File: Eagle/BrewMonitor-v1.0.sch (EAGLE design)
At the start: 14 parts, among them U1 ATMEGA328P_PDIP

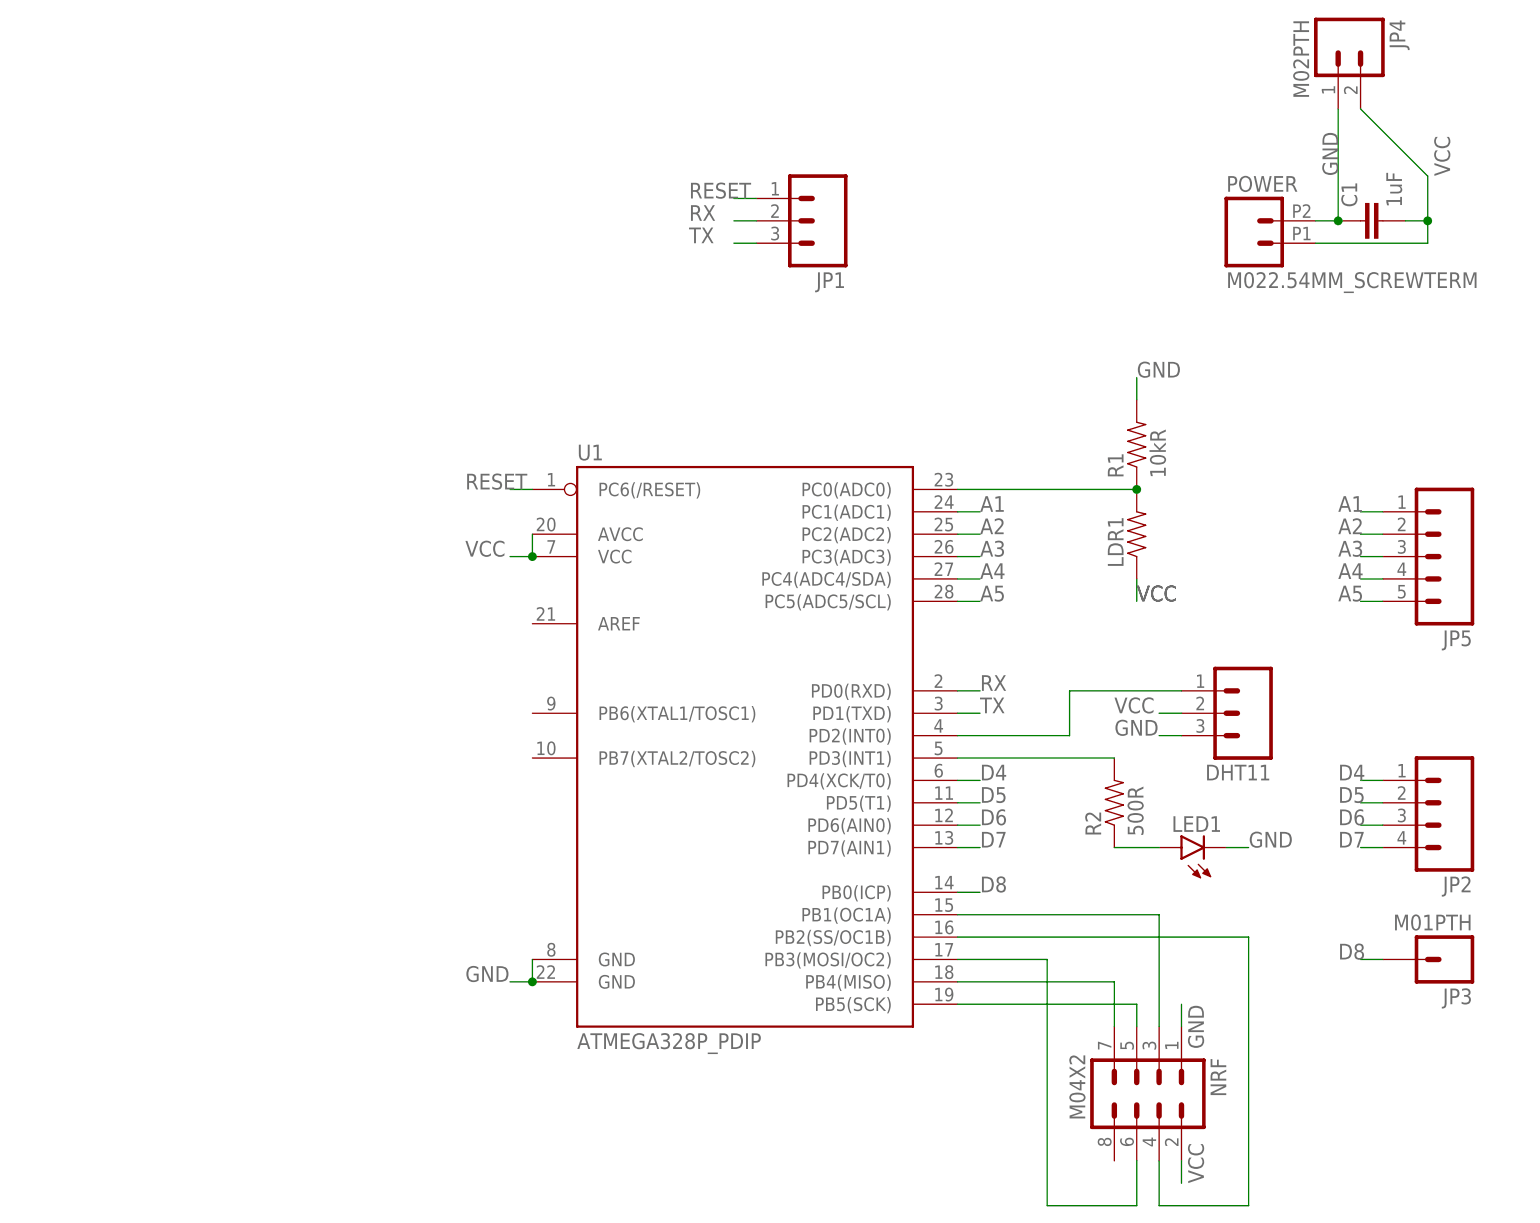
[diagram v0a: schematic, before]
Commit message: Updated Eagle Schematic for the correct parts and made net connections. The brd file still needs updating.
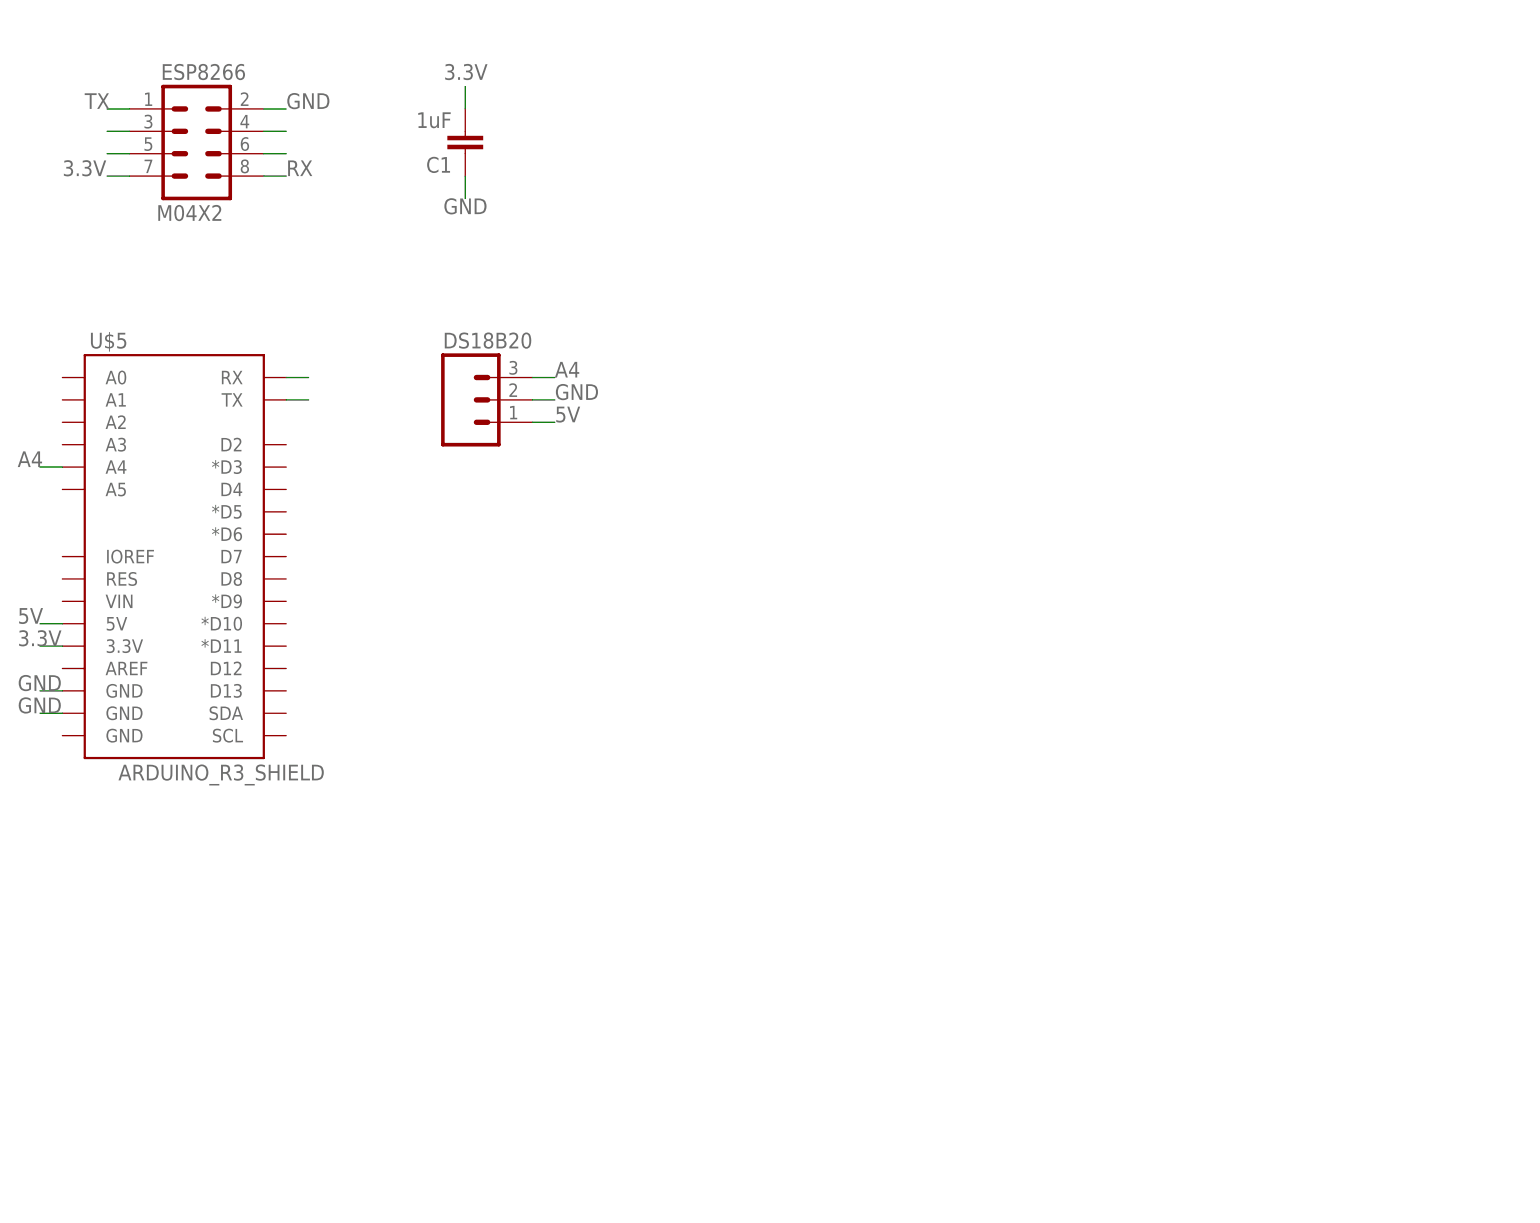
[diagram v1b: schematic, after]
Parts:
- removed DHT11, JP1: (no value), SparkFun-Connectors:M03PTH
- removed JP2: (no value), SparkFun-Connectors:M04PTH
- removed JP3: M01PTH, SparkFun-Connectors:M01PTH
- removed JP4: M02PTH, SparkFun-Connectors:M02PTH
- removed JP5: (no value), SparkFun-Connectors:M05PTH
- removed LDR1: (no value), SparkFun-Passives:RESISTORKIT
- removed LED1: (no value), SparkFun-LED:LED3MM
- removed NRF: M04X2, SparkFun-Connectors:M04X2
- removed POWER: M022.54MM_SCREWTERM, SparkFun-Connectors:M022.54MM_SCREWTERM
- removed R1: 10kR, SparkFun-Passives:RESISTORKIT
- removed R2: 500R, SparkFun-Passives:RESISTORKIT
- removed U1: ATMEGA328P_PDIP, SparkFun-DigitalIC:ATMEGA328P_PDIP
- added DS18B20: (no value), SparkFun-Connectors:M03SCREW
- added ESP8266: M04X2, SparkFun-Connectors:M04X2
- added U$5: ARDUINO_R3_SHIELD, SparkFun-Boards:ARDUINO_R3_SHIELD
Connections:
- removed net A1: JP5.1, U1.PC1(ADC1)
- removed net A2: JP5.2, U1.PC2(ADC2)
- removed net A3: JP5.3, U1.PC3(ADC3)
- removed net A5: JP5.5, U1.PC5(ADC5/SCL)
- removed net D4: JP2.1, U1.PD4(XCK/T0)
- removed net D5: JP2.2, U1.PD5(T1)
- removed net D6: JP2.3, U1.PD6(AIN0)
- removed net D7: JP2.4, U1.PD7(AIN1)
- removed net D8: JP3.1, U1.PB0(ICP)
- removed net N$1: LDR1.2, R1.1, U1.PC0(ADC0)
- removed net N$10: NRF.6, U1.PB3(MOSI/OC2)
- removed net N$2: LED1.A, R2.1
- removed net N$3: DHT11.1, U1.PD2(INT0)
- removed net N$4: R2.2, U1.PD3(INT1)
- removed net N$5: NRF.3, U1.PB1(OC1A)
- removed net N$6: NRF.4, U1.PB2(SS/OC1B)
- removed net N$7: NRF.5, U1.PB5(SCK)
- removed net N$9: NRF.7, U1.PB4(MISO)
- removed net RESET: JP1.1, U1.PC6(/RESET)
- removed net VCC: C1.2, DHT11.2, JP4.2, LDR1.1, NRF.2, POWER.1, U1.AVCC, U1.VCC
- new net 3.3V: C1.2, ESP8266.7, U$5.3.3V
- new net 5V: DS18B20.1, U$5.5V
- new net N$11: ESP8266.3
- new net N$12: ESP8266.5
- new net N$15: ESP8266.4
- new net N$16: ESP8266.6
- net A4: now also DS18B20.3, U$5.A4; no longer JP5.4, U1.PC4(ADC4/SDA)
- net GND: now also DS18B20.2, ESP8266.2, U$5.GND@1, U$5.GND@2; no longer DHT11.3, JP4.1, LED1.C, NRF.1, POWER.2, R1.2, U1.GND@1, U1.GND@2
- net RX: now also ESP8266.8, U$5.RX; no longer JP1.2, U1.PD0(RXD)
- net TX: now also ESP8266.1, U$5.TX; no longer JP1.3, U1.PD1(TXD)
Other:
- moved on the sheet: C1

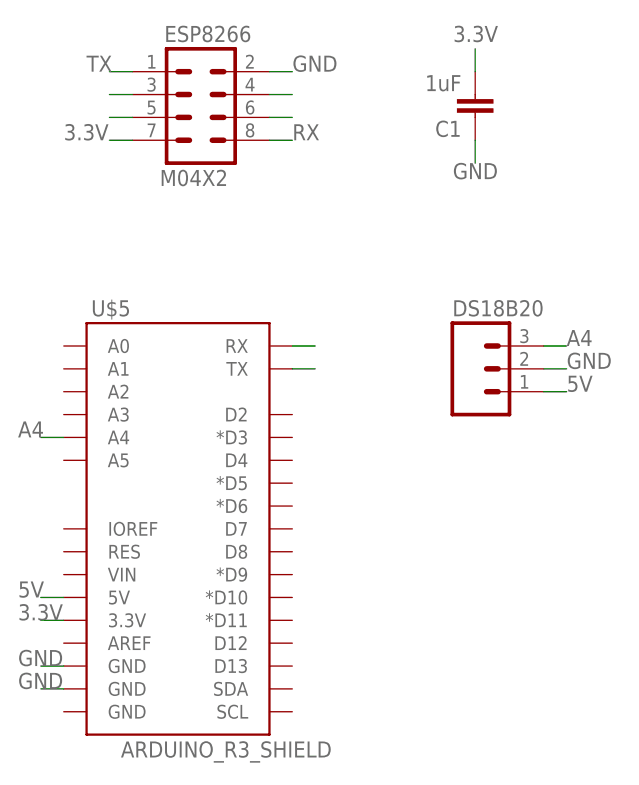
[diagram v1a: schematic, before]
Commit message: Updated Schematic and Board files. Circuit now complete.
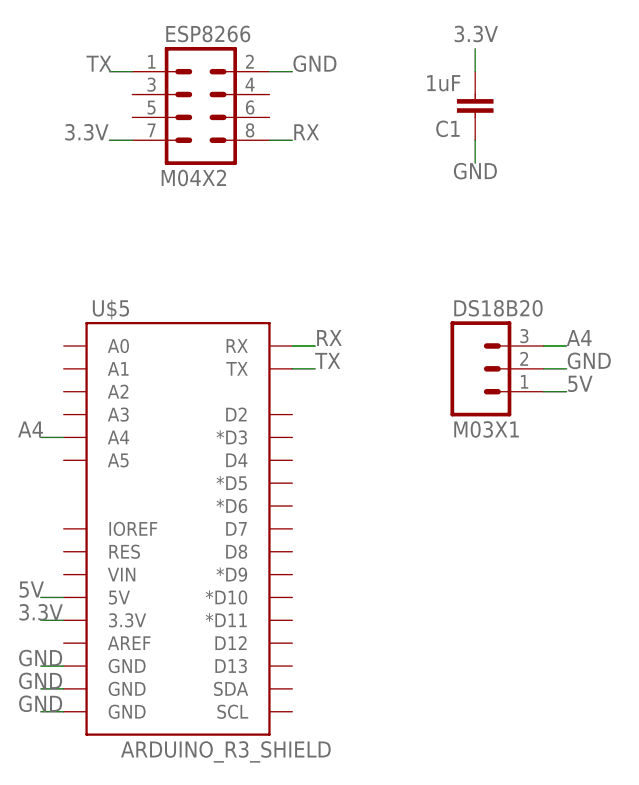
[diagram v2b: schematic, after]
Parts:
- DS18B20: value (none) -> M03X1
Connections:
- removed net N$11: ESP8266.3
- removed net N$12: ESP8266.5
- removed net N$15: ESP8266.4
- removed net N$16: ESP8266.6
- net GND: now also U$5.GND@0
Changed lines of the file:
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@@
 <part name="C1" library="SparkFun-Passives" deviceset="CAP" device="PTH" value="1uF"/>
 <part name="U$5" library="SparkFun-Boards" deviceset="ARDUINO_R3_SHIELD" device=""/>
-<part name="DS18B20" library="SparkFun-Connectors" deviceset="M03" device="SCREW"/>
+<part name="DS18B20" library="SparkFun-Connectors" deviceset="M03" device="SCREW" value="M03X1"/>
 </parts>
 <sheets>
@@
 <net name="GND" class="0">
 <segment>
-<pinref part="C1" gate="G$1" pin="1"/>
-<label x="48.26" y="106.68" size="1.778" layer="95" rot="R180"/>
-<wire x1="45.72" y1="109.22" x2="45.72" y2="106.68" width="0.1524" layer="91"/>
+<pinref part="DS18B20" gate="G$1" pin="2"/>
+<wire x1="53.34" y1="83.82" x2="55.88" y2="83.82" width="0.1524" layer="91"/>
+<label x="55.88" y="83.82" size="1.778" layer="95"/>
+</segment>
+<segment>
+<pinref part="U$5" gate="G$1" pin="GND@0"/>
+<wire x1="0" y1="45.72" x2="-2.54" y2="45.72" width="0.1524" layer="91"/>
+<label x="-5.08" y="45.72" size="1.778" layer="95"/>
 </segment>
 <segment>
@@
 </segment>
 <segment>
-<pinref part="U$5" gate="G$1" pin="GND@1"/>
-<wire x1="0" y1="48.26" x2="-2.54" y2="48.26" width="0.1524" layer="91"/>
-<label x="-5.08" y="48.26" size="1.778" layer="95"/>
+<pinref part="C1" gate="G$1" pin="1"/>
+<label x="48.26" y="106.68" size="1.778" layer="95" rot="R180"/>
+<wire x1="45.72" y1="109.22" x2="45.72" y2="106.68" width="0.1524" layer="91"/>
 </segment>
 <segment>
@@
 </segment>
 <segment>
-<pinref part="DS18B20" gate="G$1" pin="2"/>
-<wire x1="53.34" y1="83.82" x2="55.88" y2="83.82" width="0.1524" layer="91"/>
-<label x="55.88" y="83.82" size="1.778" layer="95"/>
+<pinref part="U$5" gate="G$1" pin="GND@1"/>
+<wire x1="0" y1="48.26" x2="-2.54" y2="48.26" width="0.1524" layer="91"/>
+<label x="-5.08" y="48.26" size="1.778" layer="95"/>
 </segment>
 </net>
@@
 <pinref part="U$5" gate="G$1" pin="RX"/>
 <wire x1="25.4" y1="86.36" x2="27.94" y2="86.36" width="0.1524" layer="91"/>
+<label x="27.94" y="86.36" size="1.778" layer="95"/>
 </segment>
 </net>
@@
 <pinref part="U$5" gate="G$1" pin="TX"/>
 <wire x1="25.4" y1="83.82" x2="27.94" y2="83.82" width="0.1524" layer="91"/>
-</segment>
-</net>
-<net name="N$11" class="0">
-<segment>
-<pinref part="ESP8266" gate="G$1" pin="3"/>
-<wire x1="5.08" y1="114.3" x2="7.62" y2="114.3" width="0.1524" layer="91"/>
-</segment>
-</net>
-<net name="N$12" class="0">
-<segment>
-<pinref part="ESP8266" gate="G$1" pin="5"/>
-<wire x1="5.08" y1="111.76" x2="7.62" y2="111.76" width="0.1524" layer="91"/>
+<label x="27.94" y="83.82" size="1.778" layer="95"/>
 </segment>
 </net>
@@
 </segment>
 </net>
-<net name="N$15" class="0">
-<segment>
-<pinref part="ESP8266" gate="G$1" pin="4"/>
-<wire x1="22.86" y1="114.3" x2="25.4" y2="114.3" width="0.1524" layer="91"/>
-</segment>
-</net>
-<net name="N$16" class="0">
-<segment>
-<pinref part="ESP8266" gate="G$1" pin="6"/>
-<wire x1="22.86" y1="111.76" x2="25.4" y2="111.76" width="0.1524" layer="91"/>
-</segment>
-</net>
